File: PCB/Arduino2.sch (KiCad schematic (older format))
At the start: 3 parts, among them U5 Arduino-Pro-5V

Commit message: Adding footprints cont.
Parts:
- H5: footprint (none) -> Footprints:Pin_Header_Straight_1x06_Pitch2.54mm
- U5: footprint (none) -> Footprints:ArduinoMINIPRO
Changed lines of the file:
@@
 F 0 "H5" H 4275 2450 60  0000 C CNN
 F 1 "Header1" H 4375 2375 60  0001 C CNN
-F 2 "" H 4375 2350 60  0001 C CNN
+F 2 "Footprints:Pin_Header_Straight_1x06_Pitch2.54mm" H 4375 2350 60  0001 C CNN
 F 3 "" H 4375 2350 60  0001 C CNN
 	1    4375 2350
@@
 F 0 "U5" H 4500 3100 60  0000 C CNN
 F 1 "Arduino-Pro-5V" H 4550 2950 60  0000 C CNN
-F 2 "" H 5350 3400 60  0001 C CNN
+F 2 "Footprints:ArduinoMINIPRO" H 5350 3400 60  0001 C CNN
 F 3 "" H 5350 3400 60  0001 C CNN
 	1    5050 3600

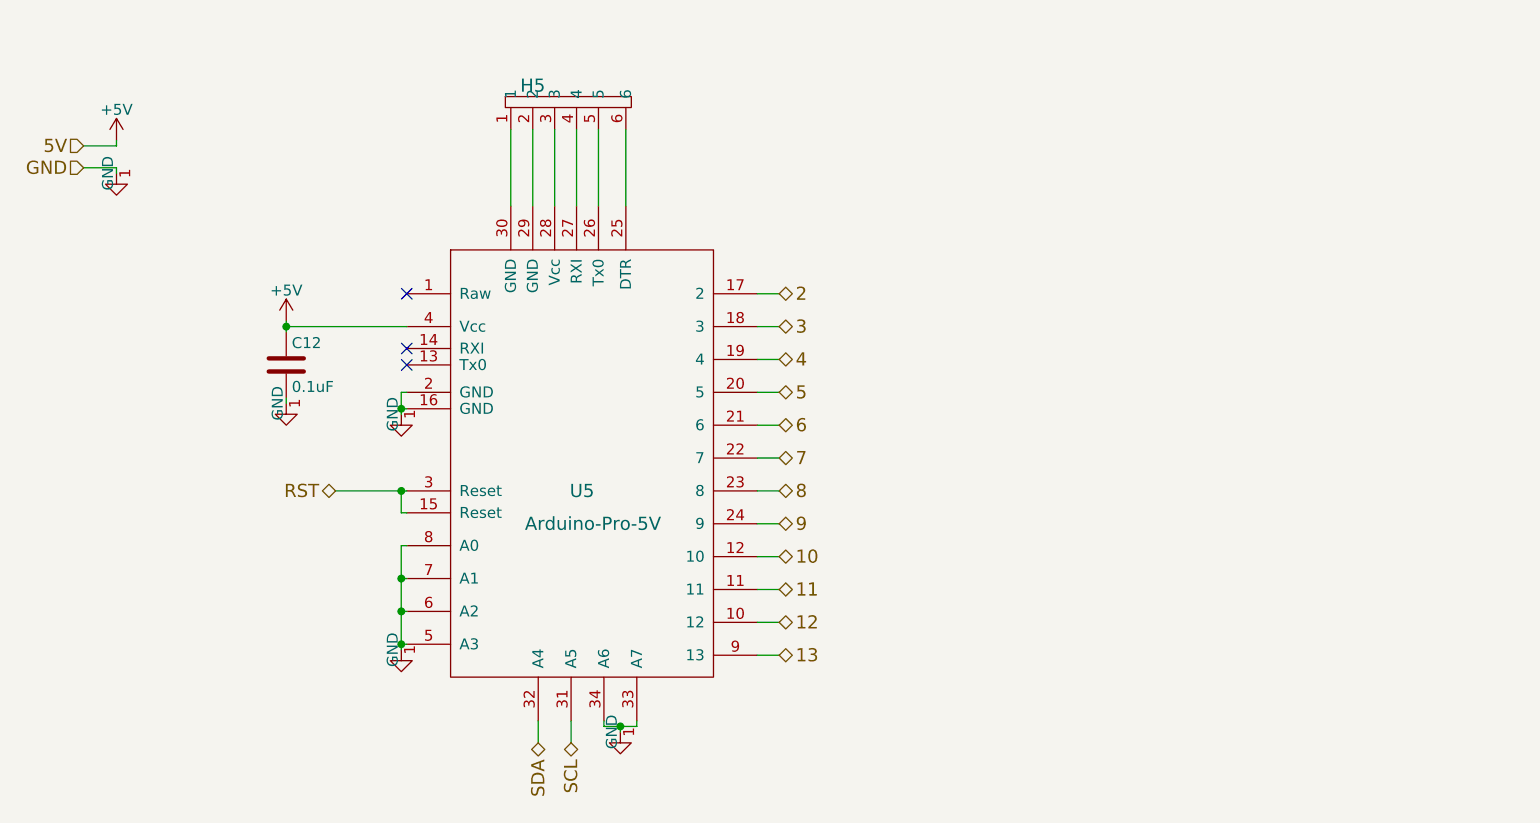
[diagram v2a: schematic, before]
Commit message: Added PCB layout
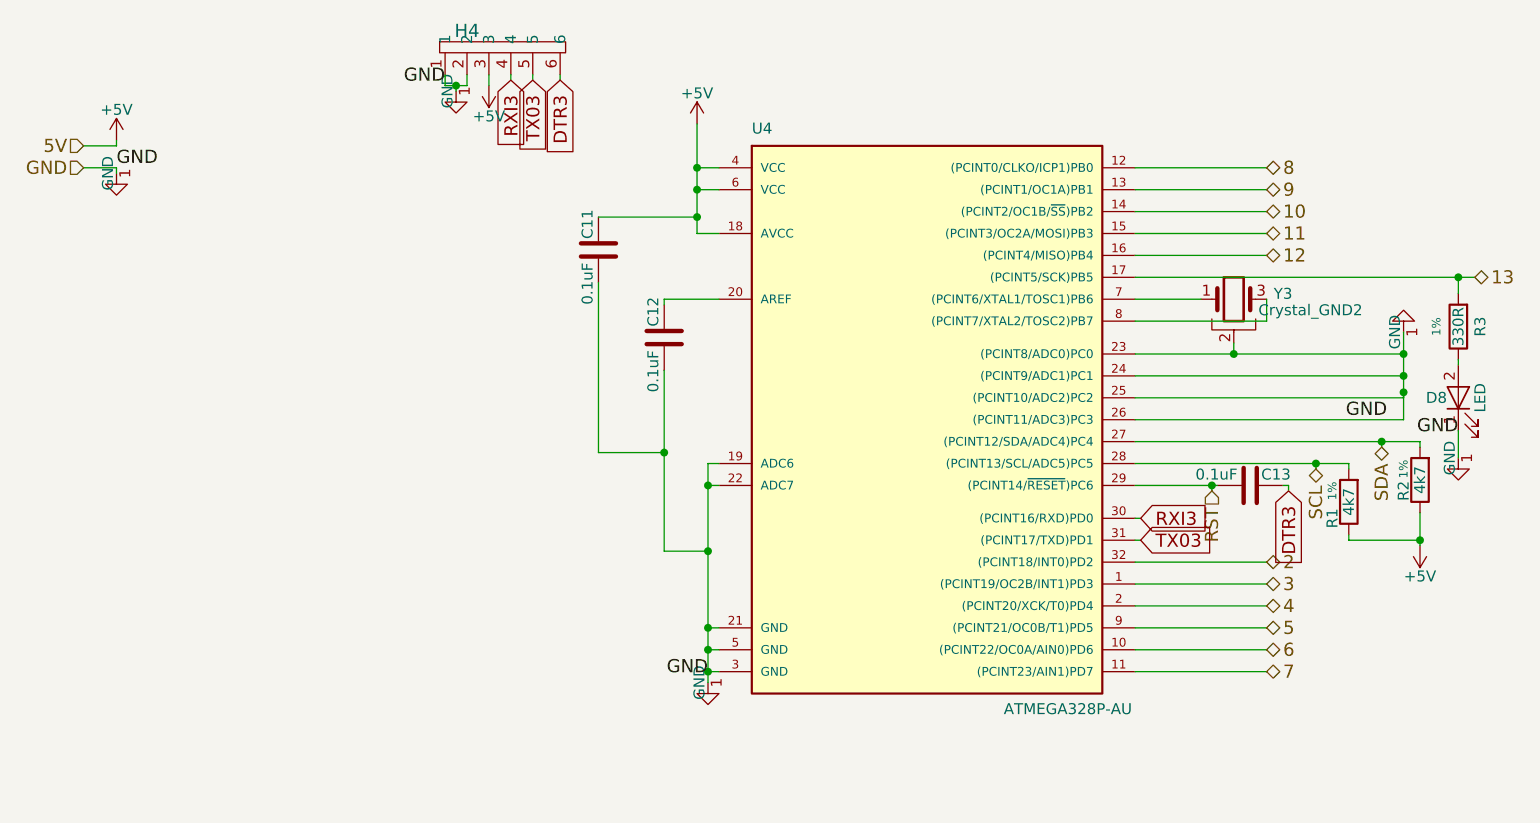
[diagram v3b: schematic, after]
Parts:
- removed H5: Header1, Footprints:Pin_Header_Straight_1x06_Pitch2.54mm, symbol Header1
- removed U5: Arduino-Pro-5V, Footprints:ArduinoMINIPRO, symbol Arduino-Pro-5V
- added C11, C13: 0.1uF, Capacitors_SMD:C_0603_HandSoldering, symbol C
- added D8: LED, LEDs:LED_0805_HandSoldering, symbol LED
- added H4: Header1, Pin_Headers:Pin_Header_Straight_1x06_Pitch2.54mm, symbol Header1
- added R1, R2: 4k7, Resistors_SMD:R_0603_HandSoldering, symbol R
- added R3: 330R, Resistors_SMD:R_0603_HandSoldering, symbol R
- added U4: ATMEGA328P-AU, Housings_QFP:TQFP-32_7x7mm_Pitch0.8mm, symbol ATMEGA328P-AU
- added Y3: Crystal_GND2, Crystals:Resonator_SMD-3pin_7.2x3.0mm_HandSoldering, symbol Crystal_GND2
- C12: footprint (none) -> Capacitors_SMD:C_0603_HandSoldering
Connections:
- net +5V: now also C11.1, H4.3, R1.1, R2.1, U4.18 (AVCC), U4.4 (VCC), U4.6 (VCC); no longer C12.1
- net 10: now also U4.14 ((PCINT2/OC1B/~SS~)PB2)
- net 11: now also U4.15 ((PCINT3/OC2A/MOSI)PB3)
- net 12: now also U4.16 ((PCINT4/MISO)PB4)
- net 13: now also R3.2, U4.17 ((PCINT5/SCK)PB5)
- net 2: now also U4.32 ((PCINT18/INT0)PD2)
- net 3: now also U4.1 ((PCINT19/OC2B/INT1)PD3)
- net 4: now also U4.2 ((PCINT20/XCK/T0)PD4)
- net 5: now also U4.9 ((PCINT21/OC0B/T1)PD5)
- net 6: now also U4.10 ((PCINT22/OC0A/AIN0)PD6)
- net 7: now also U4.11 ((PCINT23/AIN1)PD7)
- net 8: now also U4.12 ((PCINT0/CLKO/ICP1)PB0)
- net 9: now also U4.13 ((PCINT1/OC1A)PB1)
- net GND: now also C12.2, C11.2, D8.1 (K), H4.1, H4.2, U4.19 (ADC6), U4.21 (GND), U4.22 (ADC7), U4.23 ((PCINT8/ADC0)PC0), U4.24 ((PCINT9/ADC1)PC1), U4.25 ((PCINT10/ADC2)PC2), U4.26 ((PCINT11/ADC3)PC3), U4.3 (GND), U4.5 (GND), Y3.2
- net RST: now also C13.2, U4.29 ((PCINT14/~RESET~)PC6)
- net SCL: now also R1.2, U4.28 ((PCINT13/SCL/ADC5)PC5)
- net SDA: now also R2.2, U4.27 ((PCINT12/SDA/ADC4)PC4)
- new net: C12.1, U4.20 (AREF)
- new net: U4.7 ((PCINT6/XTAL1/TOSC1)PB6), Y3.1
- new net: U4.8 ((PCINT7/XTAL2/TOSC2)PB7), Y3.3
- new net: D8.2 (A), R3.1
- new net DTR3: C13.1, H4.6
- new net RXI3: H4.4, U4.30 ((PCINT16/RXD)PD0)
- new net TX03: H4.5, U4.31 ((PCINT17/TXD)PD1)
- no-connect marks 3 -> 0
